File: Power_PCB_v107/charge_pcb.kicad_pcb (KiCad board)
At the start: 2 copper layers, 128.1 x 64 mm, 48 parts, among them J1 Main_PCB2, J10 Mot_Left, J11 DC/DC1, J12 DC/DC2, J2 Battery, J3 Power Switch, J4 Mow3, J5 Main_PCB1, J6 Mow2, J7 Mow1, J8 Start, J9 Mot_Right, Q1 BC547C, Q2 IRF9540N, Q3 BC547C, Q4 IRF9540N, U1 INA226, U2 INA226, U3 INA226, U4 INA226, U5 INA226, U6 INA226

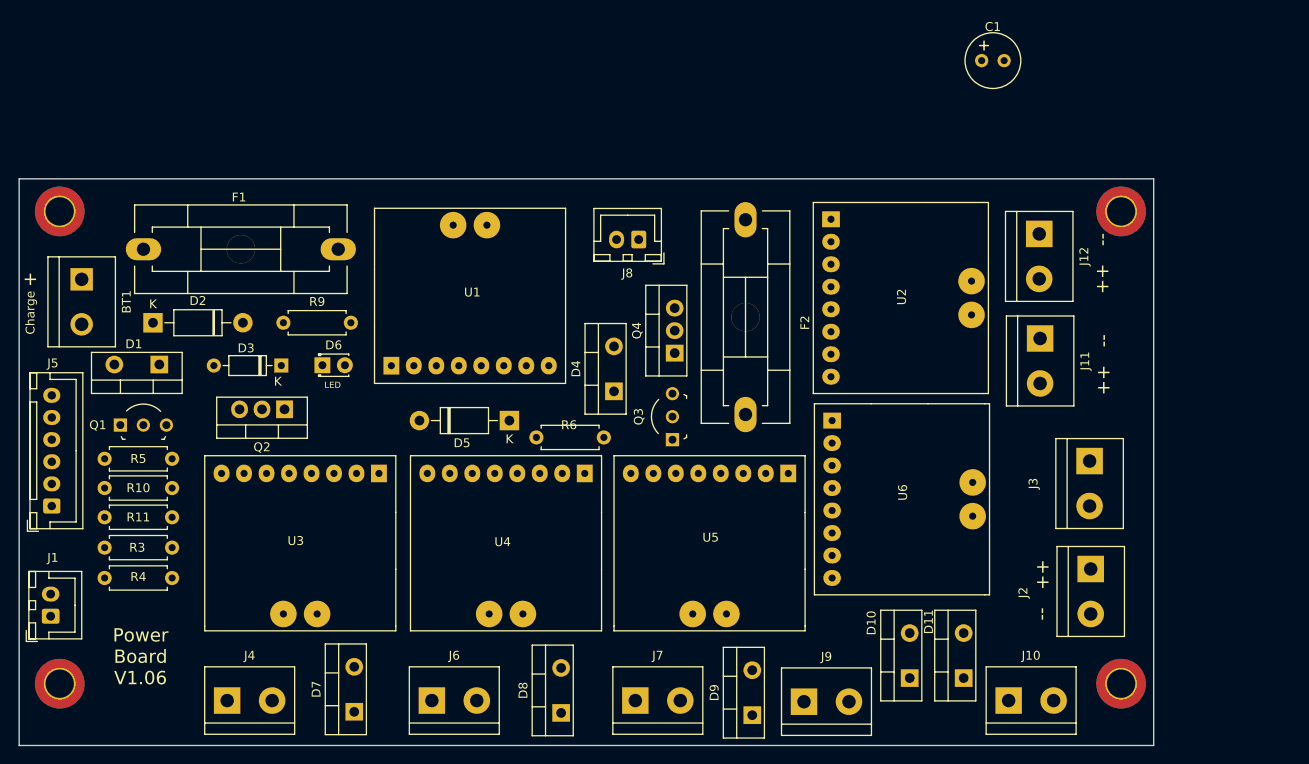
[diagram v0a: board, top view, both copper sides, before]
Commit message: Rework of chargePCB
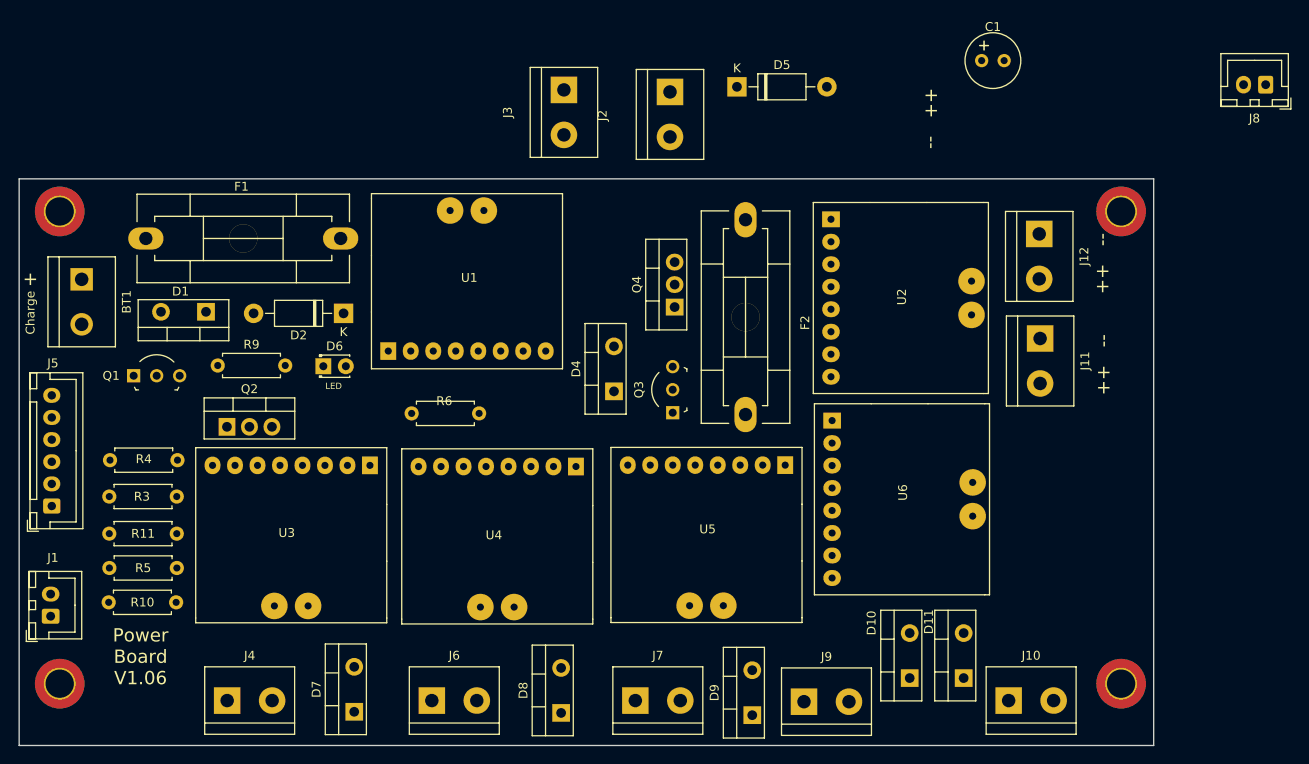
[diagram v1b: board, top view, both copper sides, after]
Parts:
- removed D3: NOT USE, Diode_THT:D_DO-35_SOD27_P7.62mm_Horizontal
- moved J8 72.9 mm to (225.5, 50.6)
- moved J3 72.7 mm to (146.2, 51.2)
- moved J2 71.8 mm to (158.2, 51.4)
- moved D5 45.6 mm to (165.8, 50.8), turned to 0 degrees
- moved D2 21.6 mm to (121.3, 76.4), turned to 180 degrees
- moved R6 14.3 mm to (129.0, 87.7)
- moved R4 13.3 mm to (102.6, 93.0)
- moved R10 12.9 mm to (94.8, 109.0)
- moved R5 12.3 mm to (94.9, 105.2)
- moved R9 8.85 mm to (107.1, 82.3)
- moved D1 7.95 mm to (105.8, 76.2)
- moved Q2 6.79 mm to (108.2, 89.2), turned to 0 degrees
- moved R3 5.79 mm to (102.5, 97.1)
- moved Q1 5.77 mm to (97.6, 83.5)
- moved Q4 5.20 mm to (158.7, 75.7)
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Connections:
- D5 pad 1: Net-(D4-Pad1) -> V_Bat
- J11 pad 2: V_Bat -> Net-(D5-Pad2)
- J12 pad 2: V_Bat -> Net-(D5-Pad2)
- Q4 pad 3: Net-(D5-Pad2) -> Net-(D4-Pad1)
- R6 pad 1: Net-(D5-Pad2) -> Net-(D4-Pad1)
- U1 pad 1: (no net) -> unconnected-(U1-Pad1)
- U1 pad 2: (no net) -> unconnected-(U1-Pad2)
- U1 pad 4: (no net) -> unconnected-(U1-Pad4)
- U2 pad 1: (no net) -> unconnected-(U2-Pad1)
- U2 pad 2: (no net) -> unconnected-(U2-Pad2)
- U2 pad 4: (no net) -> unconnected-(U2-Pad4)
- U2 pad 9: V_Bat -> Net-(D5-Pad2)
- U3 pad 1: (no net) -> unconnected-(U3-Pad1)
- U3 pad 2: (no net) -> unconnected-(U3-Pad2)
- U3 pad 4: (no net) -> unconnected-(U3-Pad4)
- U3 pad 9: V_Bat -> Net-(D5-Pad2)
- U4 pad 1: (no net) -> unconnected-(U4-Pad1)
- U4 pad 2: (no net) -> unconnected-(U4-Pad2)
- U4 pad 4: (no net) -> unconnected-(U4-Pad4)
- U4 pad 9: V_Bat -> Net-(D5-Pad2)
- U5 pad 1: (no net) -> unconnected-(U5-Pad1)
- U5 pad 2: (no net) -> unconnected-(U5-Pad2)
- U5 pad 4: (no net) -> unconnected-(U5-Pad4)
- U5 pad 9: V_Bat -> Net-(D5-Pad2)
- U6 pad 1: (no net) -> unconnected-(U6-Pad1)
- U6 pad 2: (no net) -> unconnected-(U6-Pad2)
- U6 pad 4: (no net) -> unconnected-(U6-Pad4)
- U6 pad 9: V_Bat -> Net-(D5-Pad2)
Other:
- net class +24V removed
- net class +3V removed
- net class Default removed
- board text removed: "GND"

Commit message: Rebuild Charge Board
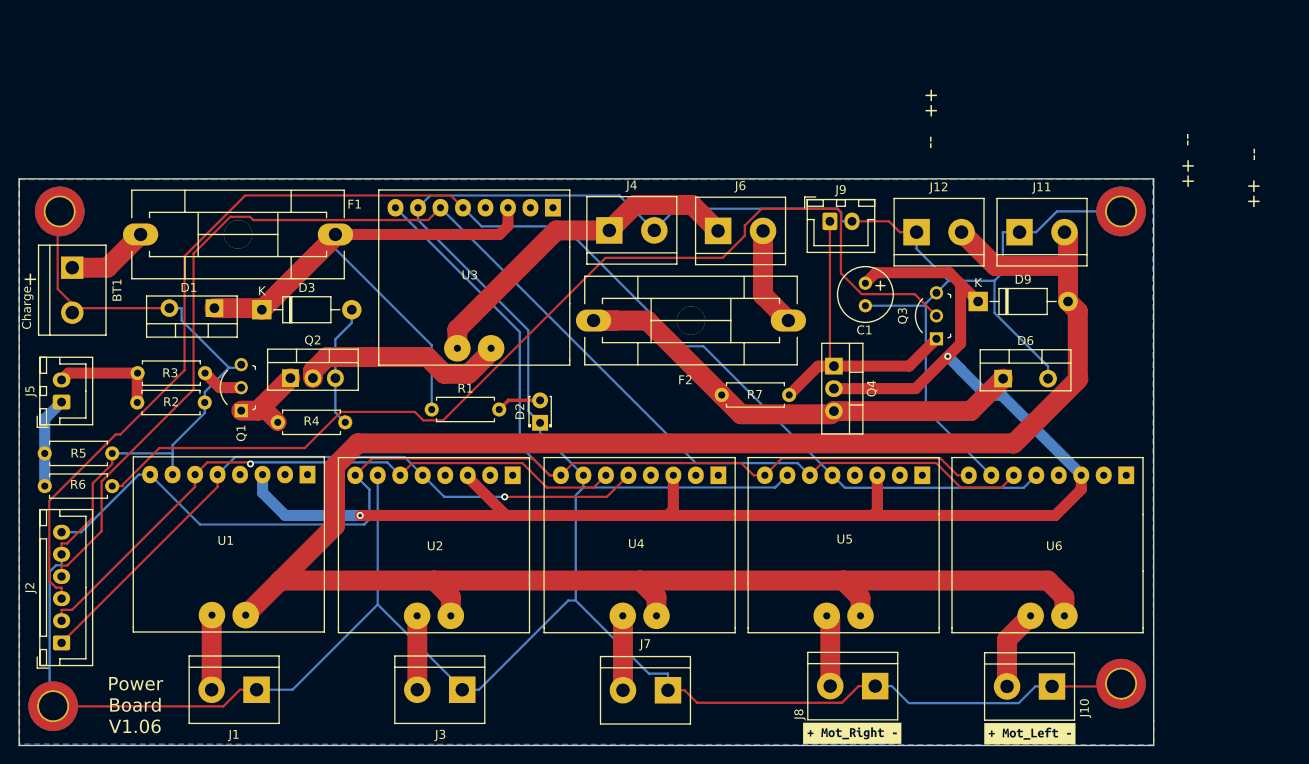
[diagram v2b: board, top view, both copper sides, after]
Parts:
- removed D10, D11, D4, D7, D8: MBR1045, Package_TO_SOT_THT:TO-220-2_Vertical
- removed D5: SB1240, Diode_THT:D_DO-41_SOD81_P10.16mm_Horizontal
- removed R10, R11: 4k7, Resistor_THT:R_Axial_DIN0207_L6.3mm_D2.5mm_P7.62mm_Horizontal
- removed R9: 4.7kO, Resistor_THT:R_Axial_DIN0207_L6.3mm_D2.5mm_P7.62mm_Horizontal
- added D3: SB1240, Diode_THT:D_DO-41_SOD81_P10.16mm_Horizontal, F.Cu at (112.1, 76.0)
- added R1: 4.7kO, Resistor_THT:R_Axial_DIN0207_L6.3mm_D2.5mm_P7.62mm_Horizontal, F.Cu at (131.3, 87.3)
- added R2: 4k7, Resistor_THT:R_Axial_DIN0207_L6.3mm_D2.5mm_P7.62mm_Horizontal, F.Cu at (98.0, 86.5)
- added R7: 4k7, Resistor_THT:R_Axial_DIN0207_L6.3mm_D2.5mm_P7.62mm_Horizontal, F.Cu at (164.1, 85.6)
- added kibuzzard-62B75E62: G***, kibuzzard-62B75E62, F.Cu at (198.9, 123.9)
- added kibuzzard-62B75EB1: G***, kibuzzard-62B75EB1, F.Cu at (178.8, 123.8)
- D2: value SB1240 -> LED; footprint Diode_THT:D_DO-41_SOD81_P10.16mm_Horizontal -> LED_THT:LED_D1.8mm_W3.3mm_H2.4mm
- D6: value LED -> MBR1045; footprint LED_THT:LED_D1.8mm_W3.3mm_H2.4mm -> Package_TO_SOT_THT:TO-220-2_Vertical
- D9: value MBR1045 -> SB1240; footprint Package_TO_SOT_THT:TO-220-2_Vertical -> Diode_THT:D_DO-41_SOD81_P10.16mm_Horizontal
- J1: value Main_PCB2 -> Mow3; footprint Connector_JST:JST_XH_B2B-XH-A_1x02_P2.50mm_Vertical -> TerminalBlock:TerminalBlock_bornier-2_P5.08mm
- J11: value DC/DC1 -> DC/DC2
- J12: value DC/DC2 -> DC/DC1
- J2: value Battery -> Main_PCB1; footprint TerminalBlock:TerminalBlock_bornier-2_P5.08mm -> Connector_JST:JST_XH_B6B-XH-A_1x06_P2.50mm_Vertical
- J3: value Power Switch -> Mow2
- J4: value Mow3 -> Battery
- J5: value Main_PCB1 -> Main_PCB2; footprint Connector_JST:JST_XH_B6B-XH-A_1x06_P2.50mm_Vertical -> Connector_JST:JST_XH_B2B-XH-A_1x02_P2.50mm_Vertical
- J6: value Mow2 -> Power Switch
- J8: value Start -> Mot_Right; footprint Connector_JST:JST_XH_B2B-XH-A_1x02_P2.50mm_Vertical -> TerminalBlock:TerminalBlock_bornier-2_P5.08mm
- J9: value Mot_Right -> Start; footprint TerminalBlock:TerminalBlock_bornier-2_P5.08mm -> Connector_JST:JST_XH_B2B-XH-A_1x02_P2.50mm_Vertical
- moved J2 92.7 mm to (89.5, 113.6), turned to 90 degrees
- moved J8 81.0 mm to (181.4, 118.5)
- moved D6 76.8 mm to (195.8, 83.8)
- moved J3 68.7 mm to (134.8, 118.9), turned to 180 degrees
- moved J4 68.4 mm to (151.4, 67.0)
- moved J6 62.1 mm to (163.7, 67.1)
- moved U2 59.3 mm to (131.6, 102.3), turned to 180 degrees
- moved J9 54.3 mm to (176.3, 66.0)
- moved D9 53.2 mm to (193.0, 75.1), turned to 0 degrees
- moved R6 42.2 mm to (87.6, 95.9)
- moved U1 39.7 mm to (108.4, 102.2), turned to 180 degrees
- moved U3 35.7 mm to (136.1, 72.1)
- moved Q3 30.9 mm to (188.3, 79.3)
- moved C1 28.4 mm to (180.3, 73.0), turned to -90 degrees
- moved D2 25.4 mm to (143.6, 88.8), turned to 90 degrees
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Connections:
- D2 pad 1: V_Charge -> GND
- D2 pad 2: Net-(Q2-Pad3) -> Net-(D2-Pad2)
- D6 pad 1: GND -> +24V
- D6 pad 2: Net-(D6-Pad2) -> GND
- D9 pad 1: Net-(D9-Pad1) -> V_Bat
- F2 pad 2: Net-(D4-Pad1) -> +24V
- J1 pad 1: pinBatterySwitch -> GND
- J1 pad 2: pinChargeEnable -> Net-(U1-Pad10)
- J10 pad 2: Net-(D11-Pad1) -> Net-(J10-Pad2)
- J11 pad 2: Net-(D5-Pad2) -> Net-(D9-Pad2)
- J12 pad 2: Net-(D5-Pad2) -> Net-(D9-Pad2)
- J2 pad 1: Net-(J2-Pad1) -> SCL1
- J2 pad 2: GND -> SDA1
- J3 pad 1: Net-(J2-Pad1) -> GND
- J3 pad 2: Net-(F2-Pad1) -> Net-(J3-Pad2)
- J4 pad 1: GND -> Net-(J4-Pad1)
- J4 pad 2: Net-(D7-Pad1) -> GND
- J5 pad 1: SCL1 -> pinBatterySwitch
- J5 pad 2: SDA1 -> pinChargeEnable
- J6 pad 1: GND -> Net-(J4-Pad1)
- J6 pad 2: Net-(D8-Pad1) -> Net-(F2-Pad1)
- J7 pad 2: Net-(D9-Pad1) -> Net-(J7-Pad2)
- J8 pad 1: Net-(J8-Pad1) -> GND
- J8 pad 2: GND -> Net-(J8-Pad2)
- J9 pad 1: GND -> Net-(J9-Pad1)
- J9 pad 2: Net-(D10-Pad1) -> GND
- Q2 pad 3: Net-(Q2-Pad3) -> Net-(D3-Pad2)
- Q3 pad 1: Net-(J8-Pad1) -> Net-(J9-Pad1)
- Q4 pad 1: Net-(J8-Pad1) -> Net-(J9-Pad1)
- Q4 pad 3: Net-(D4-Pad1) -> +24V
- R4 pad 1: Net-(Q2-Pad3) -> Net-(D3-Pad2)
- R5 pad 2: Net-(Q3-Pad2) -> GND
- R6 pad 1: Net-(D4-Pad1) -> pinBatterySwitch
- R6 pad 2: Net-(J8-Pad1) -> Net-(Q3-Pad2)
- U1 pad 10: Net-(J2-Pad1) -> Net-(U1-Pad10)
- U1 pad 3: V_Charge -> V_Bat
- U1 pad 5: SCL0 -> SCL1
- U1 pad 6: SDA0 -> SDA1
- U1 pad 9: Net-(Q2-Pad2) -> Net-(D9-Pad2)
- U2 pad 10: Net-(D11-Pad2) -> Net-(J3-Pad2)
- U2 pad 5: SCL0 -> SCL1
- U2 pad 6: SDA0 -> SDA1
- U2 pad 9: Net-(D5-Pad2) -> Net-(D9-Pad2)
- U3 pad 10: Net-(D7-Pad2) -> Net-(J4-Pad1)
- U3 pad 3: V_Bat -> V_Charge
- U3 pad 5: SCL1 -> SCL0
- U3 pad 6: SDA1 -> SDA0
- U3 pad 9: Net-(D5-Pad2) -> Net-(Q2-Pad2)
- U4 pad 10: Net-(D8-Pad2) -> Net-(J7-Pad2)
- U4 pad 9: Net-(D5-Pad2) -> Net-(D9-Pad2)
- U5 pad 10: Net-(D9-Pad2) -> Net-(J8-Pad2)
- U5 pad 5: SCL1 -> SCL0
- U5 pad 6: SDA1 -> SDA0
- U5 pad 9: Net-(D5-Pad2) -> Net-(D9-Pad2)
- U6 pad 10: Net-(D10-Pad2) -> Net-(J10-Pad2)
- U6 pad 9: Net-(D5-Pad2) -> Net-(D9-Pad2)
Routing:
- net GND: track 0.00 -> 461.8 mm
- net Net-(D9-Pad2): track 0.00 -> 245.5 mm
- net V_Bat: track 0.00 -> 172.7 mm, vias 0 -> 2
- net SCL0: track 0.00 -> 159.5 mm
- net +3V3: track 0.00 -> 158.0 mm
- net SDA0: track 0.00 -> 152.9 mm
- net Net-(Q3-Pad2): track 0.00 -> 116.7 mm
- net SCL1: track 0.00 -> 76.4 mm, vias 0 -> 1
- net SDA1: track 0.00 -> 73.5 mm, vias 0 -> 1
- net V_Charge: track 0.00 -> 63.7 mm
- net +24V: track 0.00 -> 54.9 mm
- net Net-(J4-Pad1): track 0.00 -> 38.6 mm
- net Net-(J9-Pad1): track 0.00 -> 35.6 mm
- net Net-(Q2-Pad2): track 0.00 -> 23.7 mm
- net Net-(D3-Pad2): track 0.00 -> 13.9 mm
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- added copper zone on B.Cu, net GND

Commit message: Don' know anymore
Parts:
- removed D6: MBR1045, Package_TO_SOT_THT:TO-220-2_Vertical
- removed D9: SB1240, Diode_THT:D_DO-41_SOD81_P10.16mm_Horizontal
- added D4: MBR1045, Package_TO_SOT_THT:TO-220-2_Vertical, F.Cu at (195.8, 83.7)
- added D5: SB1240, Diode_THT:D_DO-41_SOD81_P10.16mm_Horizontal, F.Cu at (193.1, 75.1)
- added JP1: Jumper_2_Open, Connector_PinHeader_2.54mm:PinHeader_1x02_P2.54mm_Vertical, F.Cu at (149.1, 85.6)
- D2: value LED -> SB1240; footprint LED_THT:LED_D1.8mm_W3.3mm_H2.4mm -> Diode_THT:D_DO-41_SOD81_P10.16mm_Horizontal
- D3: value SB1240 -> LED; footprint Diode_THT:D_DO-41_SOD81_P10.16mm_Horizontal -> LED_THT:LED_D1.8mm_W3.3mm_H2.4mm
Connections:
- C1 pad 1: V_Bat -> Net-(C1-Pad1)
- D1 pad 1: V_Charge -> Net-(D1-Pad1)
- D2 pad 1: GND -> Net-(D1-Pad1)
- D3 pad 1: V_Charge -> GND
- F1 pad 2: V_Charge -> Net-(D1-Pad1)
- F2 pad 2: +24V -> Net-(D4-Pad1)
- J11 pad 2: Net-(D9-Pad2) -> V_Bat
- J12 pad 2: Net-(D9-Pad2) -> V_Bat
- Q2 pad 3: Net-(D3-Pad2) -> Net-(D2-Pad2)
- Q4 pad 2: V_Bat -> Net-(C1-Pad1)
- Q4 pad 3: +24V -> Net-(D5-Pad2)
- R1 pad 1: V_Charge -> Net-(D2-Pad2)
- R1 pad 2: Net-(D2-Pad2) -> Net-(D3-Pad2)
- R4 pad 1: Net-(D3-Pad2) -> Net-(D2-Pad2)
- R7 pad 1: +24V -> Net-(D5-Pad2)
- U1 pad 9: Net-(D9-Pad2) -> V_Bat
- U2 pad 9: Net-(D9-Pad2) -> V_Bat
- U3 pad 3: V_Charge -> Net-(Q2-Pad2)
- U4 pad 9: Net-(D9-Pad2) -> V_Bat
- U5 pad 9: Net-(D9-Pad2) -> V_Bat
- U6 pad 9: Net-(D9-Pad2) -> V_Bat
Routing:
- net GND: track 461.8 -> 0.00 mm
- net Net-(D9-Pad2): track 245.5 -> 0.00 mm
- net V_Bat: track 172.7 -> 0.00 mm, vias 2 -> 0
- net SCL0: track 159.5 -> 0.00 mm
- net +3V3: track 158.0 -> 0.00 mm
- net SDA0: track 152.9 -> 0.00 mm
- net Net-(Q3-Pad2): track 116.7 -> 0.00 mm
- net SCL1: track 76.4 -> 0.00 mm, vias 1 -> 0
- net SDA1: track 73.5 -> 0.00 mm, vias 1 -> 0
- net V_Charge: track 63.7 -> 0.00 mm
- net +24V: track 54.9 -> 0.00 mm
- net Net-(J4-Pad1): track 38.6 -> 0.00 mm
- net Net-(J9-Pad1): track 35.6 -> 0.00 mm
- net Net-(Q2-Pad2): track 23.7 -> 0.00 mm
- net Net-(D3-Pad2): track 13.9 -> 0.00 mm
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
